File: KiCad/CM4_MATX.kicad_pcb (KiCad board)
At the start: 2 copper layers, 244 x 244 mm, 15 parts, among them IC1 PI7C9X2G404SLBFDE, IC2 USB2517-JZX, J5 1888811-1, J6 39-28-1243, J7 10018783-10113TLF

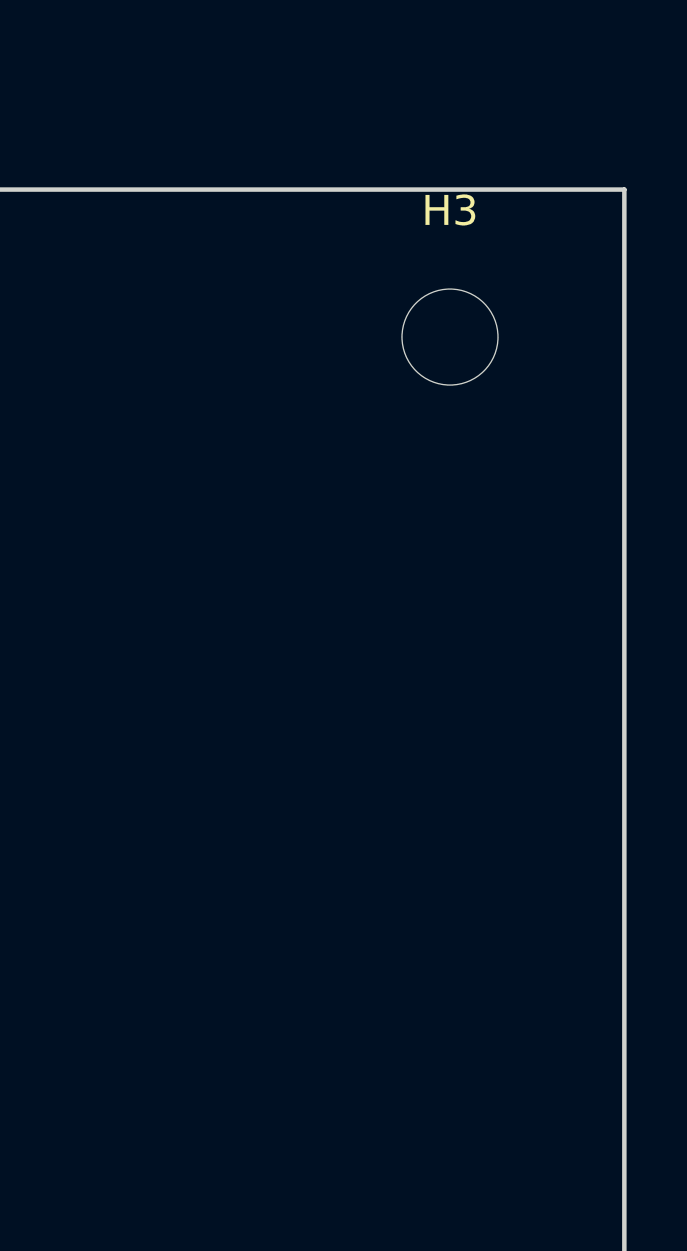
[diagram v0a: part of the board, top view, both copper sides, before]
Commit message: fixed missplaced mountinghole H3
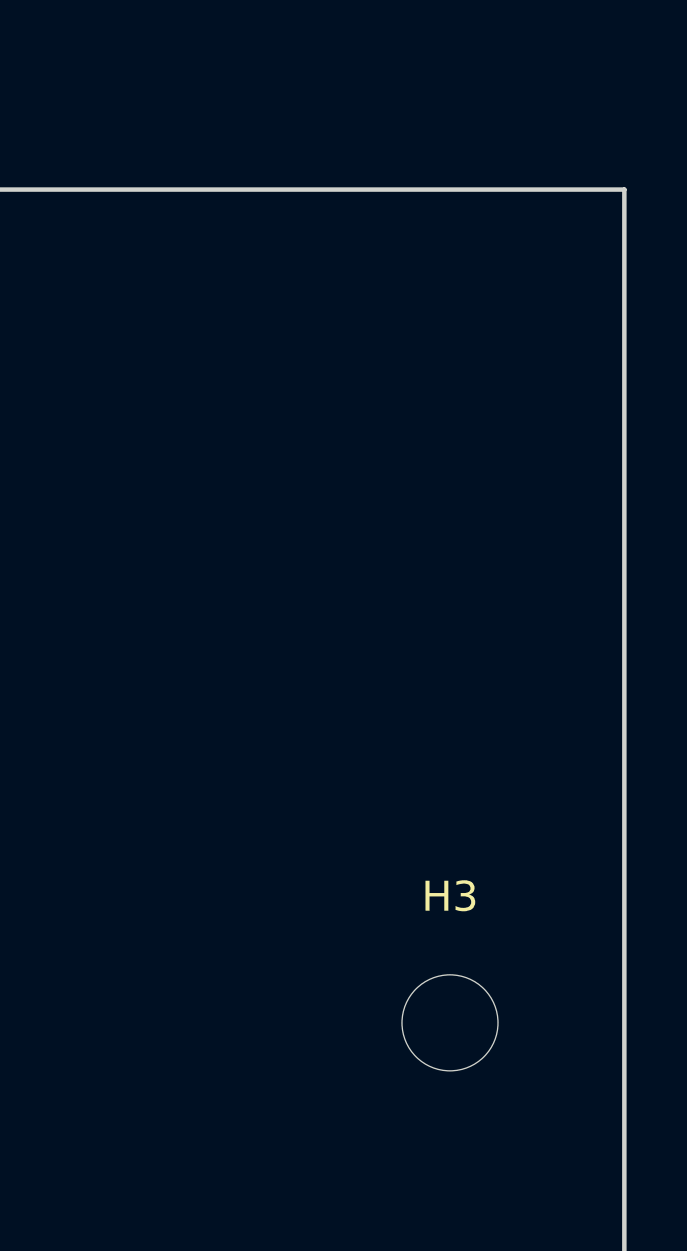
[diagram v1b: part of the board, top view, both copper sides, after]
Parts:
- moved H3 22.9 mm to (569.7, -11.6)
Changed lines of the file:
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@@
   )
   (module MountingHole:MountingHole_3.2mm_M3 (layer F.Cu)
-    (at 569.658 -34.454)
+    (at 569.658 -11.594)
     (descr "Mounting Hole 3.2mm, no annular, M3")
     (tags "mounting hole 3.2mm no annular m3")

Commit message: added rear io window placeholder
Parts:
- moved H1 333.8 mm to (35.0, 4.92)
- moved H2 333.8 mm to (80.7, 4.92)
- moved H3 333.8 mm to (238.2, 27.8)
- moved H5 333.8 mm to (35.0, 159.9)
- moved H6 333.8 mm to (80.7, 159.9)
- moved H7 333.8 mm to (238.2, 159.9)
- moved H8 333.8 mm to (80.7, 232.2)
- moved H9 333.8 mm to (238.2, 232.2)
- moved H4 333.8 mm to (14.7, 159.9)
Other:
- board text added: "REAR IO WINDOW IN CHASSIS"
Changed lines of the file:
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@@
   (general
     (thickness 1.6)
-    (drawings 4)
+    (drawings 9)
     (tracks 0)
     (zones 0)
@@
   )
   (module MountingHole:MountingHole_3.2mm_M3 (layer F.Cu)
-    (at 569.658 192.876)
+    (at 238.188 232.246)
     (descr "Mounting Hole 3.2mm, no annular, M3")
     (tags "mounting hole 3.2mm no annular m3")
@@
   )
   (module MountingHole:MountingHole_3.2mm_M3 (layer F.Cu)
-    (at 412.178 192.876)
+    (at 80.708 232.246)
     (descr "Mounting Hole 3.2mm, no annular, M3")
     (tags "mounting hole 3.2mm no annular m3")
@@
   )
   (module MountingHole:MountingHole_3.2mm_M3 (layer F.Cu)
-    (at 569.658 120.486)
+    (at 238.188 159.856)
     (descr "Mounting Hole 3.2mm, no annular, M3")
     (tags "mounting hole 3.2mm no annular m3")
@@
   )
   (module MountingHole:MountingHole_3.2mm_M3 (layer F.Cu)
-    (at 412.178 120.486)
+    (at 80.708 159.856)
     (descr "Mounting Hole 3.2mm, no annular, M3")
     (tags "mounting hole 3.2mm no annular m3")
@@
   )
   (module MountingHole:MountingHole_3.2mm_M3 (layer F.Cu)
-    (at 366.458 120.486)
+    (at 34.988 159.856)
     (descr "Mounting Hole 3.2mm, no annular, M3")
     (tags "mounting hole 3.2mm no annular m3")
@@
   )
   (module MountingHole:MountingHole_3.2mm_M3 (layer F.Cu)
-    (at 346.138 120.486)
+    (at 14.668 159.856)
     (descr "Mounting Hole 3.2mm, no annular, M3")
     (tags "mounting hole 3.2mm no annular m3")
@@
   )
   (module MountingHole:MountingHole_3.2mm_M3 (layer F.Cu)
-    (at 569.658 -11.594)
+    (at 238.188 27.776)
     (descr "Mounting Hole 3.2mm, no annular, M3")
     (tags "mounting hole 3.2mm no annular m3")
@@
   )
   (module MountingHole:MountingHole_3.2mm_M3 (layer F.Cu)
-    (at 412.178 -34.454)
+    (at 80.708 4.916)
     (descr "Mounting Hole 3.2mm, no annular, M3")
     (tags "mounting hole 3.2mm no annular m3")
@@
   )
   (module MountingHole:MountingHole_3.2mm_M3 (layer F.Cu)
-    (at 366.458 -34.454)
+    (at 34.988 4.916)
     (descr "Mounting Hole 3.2mm, no annular, M3")
     (tags "mounting hole 3.2mm no annular m3")
@@
     (pad 1 np_thru_hole circle (at 0 0) (size 3.2 3.2) (drill 3.2) (layers *.Cu *.Mask))
   )
-  (gr_line (start 331.47 -39.37) (end 331.47 204.63) (layer Edge.Cuts) (width 0.15))
-  (gr_line (start 331.47 204.63) (end 575.47 204.63) (layer Edge.Cuts) (width 0.15))
-  (gr_line (start 575.47 -39.37) (end 575.47 204.63) (layer Edge.Cuts) (width 0.15))
-  (gr_line (start 331.47 -39.37) (end 575.47 -39.37) (layer Edge.Cuts) (width 0.15))
+  (gr_text "REAR IO WINDOW IN CHASSIS" (at 99.06 -6.604) (layer Cmts.User)
+    (effects (font (size 1 1) (thickness 0.15)))
+  )
+  (gr_line (start 246.9764 -5.08) (end 246.9764 0) (layer Cmts.User) (width 0.15))
+  (gr_line (start 88.2264 -5.08) (end 88.2264 0) (layer Cmts.User) (width 0.15))
+  (gr_line (start 88.2264 -5.08) (end 246.9764 -5.08) (layer Cmts.User) (width 0.15))
+  (gr_line (start 88.2264 0) (end 246.9764 0) (layer Cmts.User) (width 0.15))
+  (gr_line (start 0 0) (end 0 244) (layer Edge.Cuts) (width 0.15))
+  (gr_line (start 0 244) (end 244 244) (layer Edge.Cuts) (width 0.15))
+  (gr_line (start 244 0) (end 244 244) (layer Edge.Cuts) (width 0.15))
+  (gr_line (start 0 0) (end 244 0) (layer Edge.Cuts) (width 0.15))
 )

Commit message: changed page size to A3
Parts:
- moved H3 35.9 mm to (263.6, 53.2)
- moved H7 35.9 mm to (263.6, 185.3)
- moved H9 35.9 mm to (263.6, 257.6)
- moved H2 35.9 mm to (106.1, 30.3)
- moved H4 35.9 mm to (40.1, 185.3)
- moved H5 35.9 mm to (60.4, 185.3)
- moved H6 35.9 mm to (106.1, 185.3)
- moved H8 35.9 mm to (106.1, 257.6)
- moved H1 35.9 mm to (60.4, 30.3)

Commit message: Lotsa changes
Added new footprints:
PCIe x1, TO-252 tab, SOT95, SOP50, SON50, Hirose FH-12-22S, 2.54mm 2x02 and 2x05 headers
Added new models:
Hirose FH-12-22S, FSUSB42MUX, MIC2019YM6-TR, TPS6206
Re-did ATX connector symbol wiring
Begun wiring PI7C PCI-e switch
Wired USB2517 hub
Begun adding MIC2019YM6 current limiters.
Added TODO lists to each page to help new contributors
Begun placing PCB footprints and descriptors
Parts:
- removed the IC2 at (236.6, -40.2)
- added IC1: USB2517-JZX, CM4_MATX:QFN50P900X900X100-65N-D, F.Cu at (102.1, 129.3)
- added J1: Conn_02x02_Odd_Even, CM4_MATX:PinHeader_2x02_P2.54mm_Vertical, F.Cu at (184.2, 97.2)
- added J10: 72309-8014BLF, CM4_MATX:723098014BLF, F.Cu at (41.8, 69.8)
- added J11: 10104110-0001LF, CM4_MATX:101041100001LF, F.Cu at (29.0, 57.4)
- added J12: SS-52100-002, CM4_MATX:SS52100002, F.Cu at (263.3, 274.6)
- added J13: 10018783-11200TLF, _LibLoader:1001878410200TLF, F.Cu at (58.2, 205.7)
- added J14: 10018783-10113TLF, CM4_MATX:10018783-10113TLF, F.Cu at (45.5, 225.8)
- added J15: 10018783-10113TLF, CM4_MATX:10018783-10113TLF, F.Cu at (45.0, 245.1)
- added J2: Conn_01x22_Female, CM4_MATX:Hirose_FH12-22S-0.5SH_1x22-1MP_P0.50mm_Horizontal, F.Cu at (174.5, 73.2)
- added J3: Conn_01x22_Female, CM4_MATX:Hirose_FH12-22S-0.5SH_1x22-1MP_P0.50mm_Horizontal, F.Cu at (174.6, 87.0)
- added J4: Conn_01x22_Female, CM4_MATX:Hirose_FH12-22S-0.5SH_1x22-1MP_P0.50mm_Horizontal, F.Cu at (196.5, 73.2)
- added J8: Conn_02x05_Odd_Even, CM4_MATX:PinHeader_2x05_P2.54mm_Vertical, F.Cu at (217.9, 275.5)
- added J9: Conn_02x05_Odd_Even, CM4_MATX:PinHeader_2x05_P2.54mm_Vertical, F.Cu at (234.1, 275.5)
- added U1: MIC2019YM6-TR, _LibLoader:SOT95P280X145-6N, F.Cu at (47.5, 67.8)
- added U2: MIC2019YM6-TR, _LibLoader:SOT95P280X145-6N, F.Cu at (47.5, 79.8)
- added U3: FSUSB42MUX, _LibLoader:SOP50P490X110-10N, F.Cu at (91.4, 125.7)
- added U4: AP7363-10D, CM4_MATX:TO-252-3_TabPin2, F.Cu at (94.3, 163.8)
- H1, H2, H3, H4, H5, H6, H7, H8, H9: footprint MountingHole:MountingHole_3.2mm_M3 -> MountingHole:MountingHole_3.2mm_M3_Pad_Via
- J5: value 1888811-1 -> Conn_01x22_Female; footprint CM4_MATX:TE_1888811-1 -> CM4_MATX:Hirose_FH12-22S-0.5SH_1x22-1MP_P0.50mm_Horizontal
- J6: value 39-28-1243 -> 1888811-1; footprint CM4_MATX:SHDR24W125P550X420_2X12_5160X960X1310P -> CM4_MATX:TE_1888811-1
- J7: value 10018783-10113TLF -> 39-28-1243; footprint CM4_MATX:10018783-10113TLF -> CM4_MATX:SHDR24W125P550X420_2X12_5160X960X1310P
- moved IC2 275.9 mm to (65.9, 166.4)
- moved J7 241.6 mm to (261.6, 125.2), turned to 90 degrees
- moved J5 229.5 mm to (196.5, 87.0)
- moved H9 217.8 mm to (258.2, 39.9)
- moved H1 214.9 mm to (30.8, 243.1)
- moved H3 210.3 mm to (53.7, 39.9)
- moved J6 191.6 mm to (39.5, 94.0), turned to 270 degrees
- moved H2 183.3 mm to (30.8, 197.4)
- moved Module1 179.1 mm to (142.0, 62.2), turned to 180 degrees
- moved H4 165.4 mm to (185.8, 263.5)
- moved H7 164.8 mm to (185.8, 39.9)
- moved H8 163.5 mm to (258.2, 197.4)
- moved H5 138.1 mm to (185.8, 243.1)
- moved H6 80.6 mm to (185.8, 197.4)
- renumbered IC1 to IC2
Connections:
- net /CM4_HighSpeed/PCIe_nRST renamed /CM4_HighSpeed/PCIE_NRST
- net Net-(IC1-Pad127) renamed /CM4_HighSpeed/PCIE_RX_N
- net Net-(IC1-Pad45) renamed /PCIe_Switch/PCIE1_IMP
- net Net-(IC1-Pad46) renamed /PCIe_Switch/PCIE2_IMP
- net Net-(IC1-Pad47) renamed /PCIe_Switch/PCIE3_IMP
- IC2 pad 1: Net-(IC1-Pad1) -> /PCIe_Switch/VDDR
- IC2 pad 100: Net-(IC1-Pad100) -> /PCIe_Ports/PCIE1_TX_P
- IC2 pad 101: Net-(IC1-Pad101) -> /PCIe_Ports/PCIE1_TX_N
- IC2 pad 102: Net-(IC1-Pad102) -> /PCIe_Ports/PCIE2_RX_P
- IC2 pad 103: Net-(IC1-Pad103) -> /PCIe_Ports/PCIE2_RX_N
- IC2 pad 104: Net-(IC1-Pad104) -> GND
- IC2 pad 106: Net-(IC1-Pad106) -> /PCIe_Ports/PCIE2_TX_P
- IC2 pad 107: Net-(IC1-Pad107) -> /PCIe_Ports/PCIE2_TX_N
- IC2 pad 11: Net-(IC1-Pad11) -> GND
- IC2 pad 110: Net-(IC1-Pad110) -> /CM4_HighSpeed/PCIE_CLK_P
- IC2 pad 111: Net-(IC1-Pad111) -> /CM4_HighSpeed/PCIE_CLK_N
- IC2 pad 117: Net-(IC1-Pad117) -> /PCIe_Ports/PCIE3_TX_N
- IC2 pad 118: Net-(IC1-Pad118) -> /PCIe_Ports/PCIE3_TX_P
- IC2 pad 12: Net-(IC1-Pad12) -> GND
- IC2 pad 120: Net-(IC1-Pad120) -> GND
- IC2 pad 121: Net-(IC1-Pad121) -> /PCIe_Ports/PCIE3_RX_N
- IC2 pad 122: Net-(IC1-Pad122) -> /PCIe_Ports/PCIE3_RX_P
- IC2 pad 123: Net-(IC1-Pad123) -> /CM4_HighSpeed/PCIE_TX_N
- IC2 pad 124: Net-(IC1-Pad124) -> /CM4_HighSpeed/PCIE_TX_P
- IC2 pad 126: Net-(IC1-Pad126) -> GND
- IC2 pad 128: Net-(IC1-Pad128) -> /CM4_HighSpeed/PCIE_RX_P
- IC2 pad 129: Net-(IC1-Pad129) -> GND
- IC2 pad 19: Net-(IC1-Pad19) -> /PCIe_Ports/PCIE1_PRSNT
- IC2 pad 2: Net-(IC1-Pad2) -> GND
- IC2 pad 20: Net-(IC1-Pad20) -> /PCIe_Ports/PCIE2_PRSNT
- IC2 pad 21: Net-(IC1-Pad21) -> /PCIe_Ports/PCIE3_PRSNT
- IC2 pad 23: Net-(IC1-Pad23) -> /PCIe_Switch/VDDC
- IC2 pad 29: Net-(IC1-Pad29) -> /PCIe_Switch/VDDC
- IC2 pad 3: Net-(IC1-Pad3) -> /PCIe_Switch/VDDC
- IC2 pad 30: Net-(IC1-Pad30) -> GND
- IC2 pad 31: Net-(IC1-Pad31) -> /PCIe_Switch/VDDC
- IC2 pad 32: Net-(IC1-Pad32) -> GND
- IC2 pad 34: Net-(IC1-Pad34) -> GND
- IC2 pad 4: Net-(IC1-Pad4) -> GND
- IC2 pad 40: Net-(IC1-Pad40) -> /PCIe_Switch/VDDC
- IC2 pad 41: Net-(IC1-Pad41) -> GND
- IC2 pad 5: Net-(IC1-Pad5) -> /PCIe_Ports/PCIE1_PERST
- IC2 pad 50: Net-(IC1-Pad50) -> GND
- IC2 pad 55: Net-(IC1-Pad55) -> /PCIe_Switch/VDDC
- IC2 pad 56: Net-(IC1-Pad56) -> GND
- IC2 pad 6: Net-(IC1-Pad6) -> /PCIe_Ports/PCIE2_PERST
- IC2 pad 61: Net-(IC1-Pad61) -> GND
- IC2 pad 62: Net-(IC1-Pad62) -> /PCIe_Switch/VDDC
- IC2 pad 63: Net-(IC1-Pad63) -> GND
- IC2 pad 65: Net-(IC1-Pad65) -> /PCIe_Switch/VDDC
- IC2 pad 66: Net-(IC1-Pad66) -> GND
- IC2 pad 7: Net-(IC1-Pad7) -> /PCIe_Ports/PCIE3_PERST
- IC2 pad 75: Net-(IC1-Pad75) -> /PCIe_Ports/PCIE3_CLK_N
- IC2 pad 76: Net-(IC1-Pad76) -> /PCIe_Ports/PCIE3_CLK_P
- IC2 pad 77: Net-(IC1-Pad77) -> /PCIe_Ports/PCIE2_CLK_N
- IC2 pad 78: Net-(IC1-Pad78) -> /PCIe_Ports/PCIE2_CLK_P
- IC2 pad 8: Net-(IC1-Pad8) -> /PCIe_Switch/VDDR
- IC2 pad 80: Net-(IC1-Pad80) -> /PCIe_Ports/PCIE1_CLK_N
- IC2 pad 81: Net-(IC1-Pad81) -> /PCIe_Ports/PCIE1_CLK_P
- IC2 pad 87: Net-(IC1-Pad87) -> GND
- IC2 pad 90: Net-(IC1-Pad90) -> GND
- IC2 pad 91: Net-(IC1-Pad91) -> /PCIe_Switch/VDDC
- IC2 pad 95: Net-(IC1-Pad95) -> GND
- IC2 pad 97: Net-(IC1-Pad97) -> /PCIe_Ports/PCIE1_RX_P
- IC2 pad 98: Net-(IC1-Pad98) -> /PCIe_Ports/PCIE1_RX_N
- Module1 pad 101: /CM4_HighSpeed/USBOTG_ID -> /USB2_HUB/USBOTG
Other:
- board text added: "5v|5v"
- board text added: "COMPONENT PLACEMENT NOT FINAL"
- board text added: "Camera Headers"
- board text added: "Camera0"
- board text added: "Camera1"
- board text added: "Display Headers"
- board text added: "Display0"
- board text added: "Display1"
- board text added: "GND|GND"
- board text added: "Jumpers to be fitted if Camera0 or Display0 are used"
- board text added: "NC|NC"
- board text added: "USB3N|USB4N"
- board text added: "USB3P|USB4P"
- board text added: "USB5N|USB6N"
- board text added: "USB5P|USB6P"

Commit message: Clean up references to _LibLoader library
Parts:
- J13: footprint _LibLoader:1001878410200TLF -> CM4_MATX:1001878410200TLF
- U1, U2: footprint _LibLoader:SOT95P280X145-6N -> CM4_MATX:SOT95P280X145-6N
- U3: footprint _LibLoader:SOP50P490X110-10N -> CM4_MATX:SOP50P490X110-10N

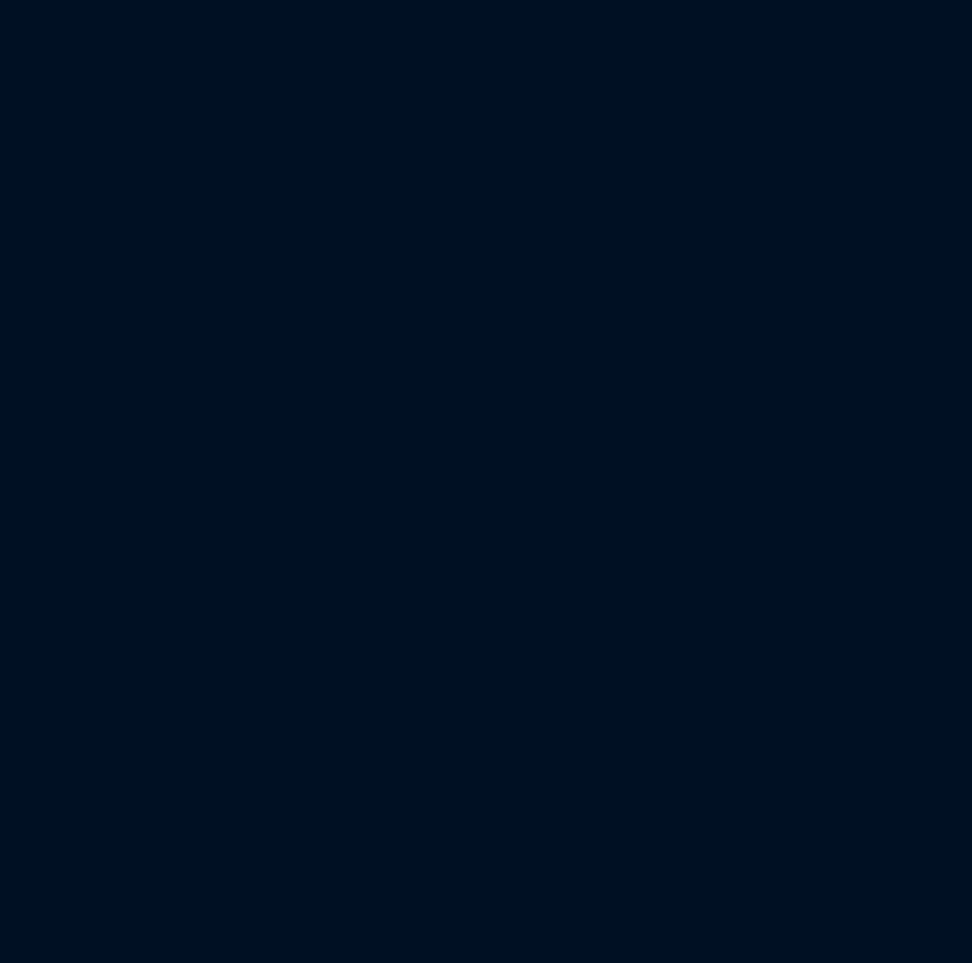
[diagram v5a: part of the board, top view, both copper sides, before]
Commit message: placed components as a functional group
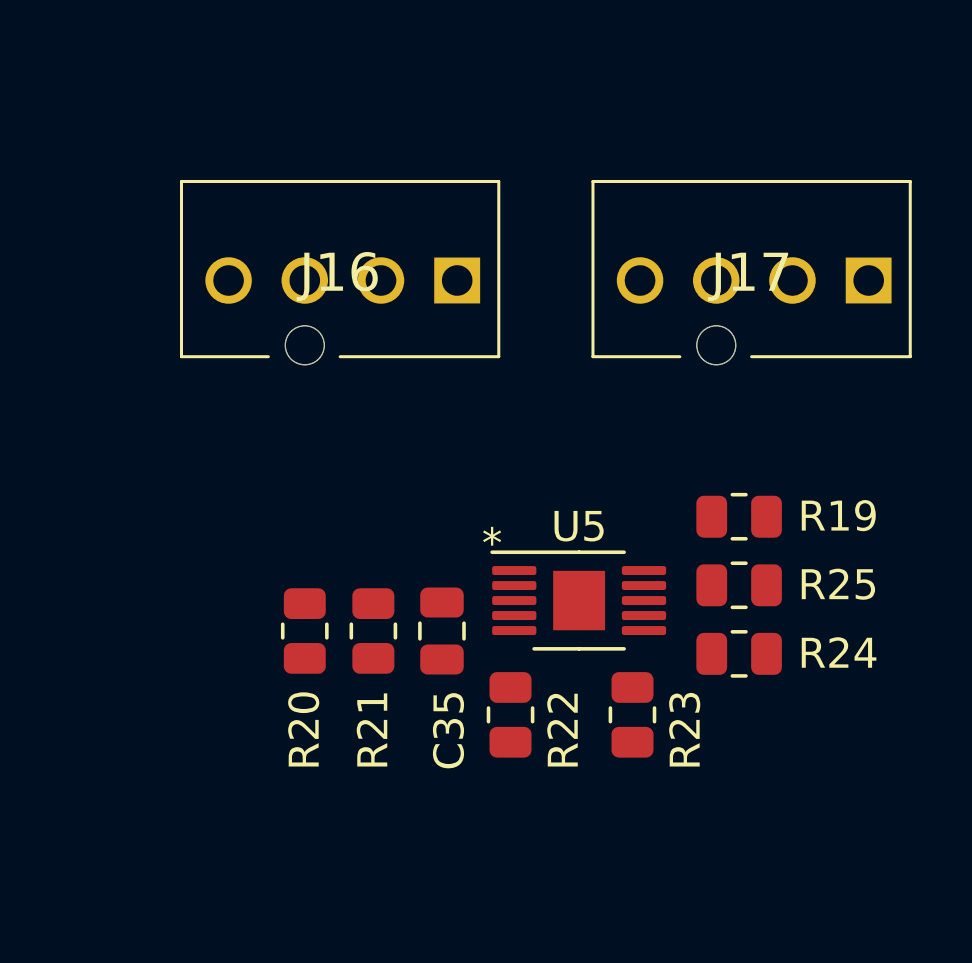
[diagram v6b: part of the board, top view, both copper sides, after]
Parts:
- added C35: C100n, CM4_MATX:C_0805_2012Metric, F.Cu at (309.1, 57.4)
- added J16: 47053-1000, CM4_MATX:470531000, F.Cu at (309.6, 45.7)
- added J17: 47053-1000, CM4_MATX:470531000, F.Cu at (323.3, 45.7)
- added R19: R10k, CM4_MATX:R_0805_2012Metric, F.Cu at (319.0, 53.6)
- added R20: R10k, CM4_MATX:R_0805_2012Metric, F.Cu at (304.5, 57.4)
- added R21: R10k, CM4_MATX:R_0805_2012Metric, F.Cu at (306.8, 57.4)
- added R22: R10k, CM4_MATX:R_0805_2012Metric, F.Cu at (311.4, 60.2)
- added R23: R10k, CM4_MATX:R_0805_2012Metric, F.Cu at (315.5, 60.2)
- added R24: R10k, CM4_MATX:R_0805_2012Metric, F.Cu at (319.0, 58.2)
- added R25: R10k, CM4_MATX:R_0805_2012Metric, F.Cu at (319.0, 55.9)
- added U5: EMC2302, CM4_MATX:MSOP-10-1EP_3x3mm_P0.5mm_EP1.73x1.98mm, F.Cu at (313.7, 56.4)
